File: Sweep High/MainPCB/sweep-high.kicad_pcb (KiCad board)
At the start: 2 copper layers, 229.5 x 95.2 mm, 64 parts, among them J1 AudioJack4dpb, J2 AudioJack4dpb, SW10 SW_Push, SW11 SW_Push, SW11_r1 SW_Push, SW12 SW_Push, SW12_r1 SW_Push, SW13_r1 SW_Push, SW14 SW_Push, SW15 SW_Push, SW15_r1 SW_Push, SW16 SW_Push, SW16_r1 SW_Push, SW17 SW_Push, SW17_r1 SW_Push, SW18 SW_Push, SW18_r1 SW_Push, SW2 SW_Push, SW2 SW_SPDT, SW20 SW_Push, SW20_r1 SW_Push, SW21 SW_Push, SW21_r1 SW_Push, SW2_r1 SW_Push, SW3 SW_Push, SW3_r1 SW_Push, SW4 SW_Push, SW4_r1 SW_Push, SW5 SW_Push, SW5_r1 SW_Push, SW6 SW_Push, SW6_r1 SW_Push, SW7_r1 SW_Push, SW8 SW_Push, SW8_r1 SW_Push, SW9 SW_Push, SW9_r1 SW_Push, U1 ProMicro-kbd, U2 ProMicro-kbd

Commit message: lots of worky
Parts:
- removed the H2 at (113.9, 55.8)
- removed H4: MountingHole, MountingHole:MountingHole_3.7mm
- removed the H5 at (54.2, 64.4)
- removed the H6 at (98.9, 119.8)
- removed the H8 at (62.1, 115.5)
- removed the SW2 at (140.6, 84.0)
- removed the SW2 at (160.9, 84.5)
- removed SW20_r1, SW21_r1: SW_Push, * duckyb-collection:keyswitch_cherrymx_alps_choc12_slots_1u
- added H0: MountingHole, MountingHole:MountingHole_3.2mm_M3, F.Cu at (99.4, 127.7)
- added H2: MountingHole, MountingHole:MountingHole_2.2mm_M2, F.Cu at (37.1, 242.3)
- added H2: MountingHole, MountingHole:MountingHole_3.2mm_M3, F.Cu at (112.1, 56.6)
- added H5: MountingHole, MountingHole:MountingHole_2.2mm_M2, F.Cu at (-21.6, 252.4)
- added H5: MountingHole, MountingHole:MountingHole_2.2mm_M2, B.Cu at (188.5, 56.6)
- added H6: MountingHole, MountingHole:MountingHole_2.2mm_M2, F.Cu at (24.4, 313.4)
- added H6: MountingHole, MountingHole:MountingHole_2.2mm_M2, B.Cu at (247.2, 66.7)
- added H8: MountingHole, MountingHole:MountingHole_2.2mm_M2, F.Cu at (-19.4, 307.3)
- added H8: MountingHole, MountingHole:MountingHole_2.2mm_M2, B.Cu at (245.0, 121.6)
- added SW10: SW_Push, Kailh:SW_PG1350_cut, F.Cu at (7.97, 263.6)
- added SW10_r1: SW_Push, kbd:CherryMX_Choc_1u, F.Cu at (169.3, 132.5)
- added SW11: SW_Push, Kailh:SW_PG1350_cut, F.Cu at (27.0, 268.2)
- added SW12: SW_Push, Kailh:SW_PG1350_cut, F.Cu at (45.9, 270.7)
- added SW14: SW_Push, Kailh:SW_PG1350_cut, F.Cu at (-30.0, 300.7)
- added SW14_r1: SW_Push, kbd:CherryMX_Choc_1u, F.Cu at (189.2, 124.4)
- added SW15: SW_Push, Kailh:SW_PG1350_cut, F.Cu at (-11.0, 288.9)
- added SW16: SW_Push, Kailh:SW_PG1350_cut, F.Cu at (7.97, 282.6)
- added SW17: SW_Push, Kailh:SW_PG1350_cut, F.Cu at (27.0, 287.2)
- added SW18: SW_Push, Kailh:SW_PG1350_cut, F.Cu at (45.9, 289.8)
- added SW2: SW_Push, Kailh:SW_PG1350_cut, F.Cu at (-30.0, 262.7)
- added SW2: SW_Push, Kailh:SW_PG1350_cut, F.Cu at (45.0, 77.0)
- added SW2: SW_Push, Kailh:SW_PG1350_cut, B.Cu at (255.6, 77.0)
- added SW20: SW_Push, Kailh:SW_PG1350_cut, F.Cu at (55.9, 318.2)
- added SW21: SW_Push, Kailh:SW_PG1350_cut, F.Cu at (36.2, 310.0)
- added SW3: SW_Push, Kailh:SW_PG1350_cut, F.Cu at (-11.0, 250.7)
- added SW4: SW_Push, Kailh:SW_PG1350_cut, F.Cu at (7.97, 244.6)
- added SW5: SW_Push, Kailh:SW_PG1350_cut, F.Cu at (27.0, 249.2)
- added SW6: SW_Push, Kailh:SW_PG1350_cut, F.Cu at (46.0, 251.7)
- added SW8: SW_Push, Kailh:SW_PG1350_cut, F.Cu at (-30.0, 281.7)
- added SW9: SW_Push, Kailh:SW_PG1350_cut, F.Cu at (-11.0, 269.8)
- ?: moved to B.Cu
- Bat+1, BatGND4: renamed from B-; footprint kbd:1pin_conn -> Connector_Pin:Pin_D1.4mm_L8.5mm_W2.8mm_FlatFork
- Bat+r1, BatGND1: renamed from B+; footprint kbd:1pin_conn -> Connector_Pin:Pin_D1.4mm_L8.5mm_W2.8mm_FlatFork
- H1, H3: footprint MountingHole:MountingHole_3.7mm -> MountingHole:MountingHole_3.2mm_M3
- H7: footprint MountingHole:MountingHole_3.7mm -> MountingHole:MountingHole_2.2mm_M2; moved to B.Cu
- J1, J2: footprint Kailh:TRRS-PJ-DPB2 -> Connector_Audio:Jack_3.5mm_PJ320D_Horizontal
- RSW1 (x2), RSW2 (x2): footprint kbd:SW_SPST_B3U-1000P -> Button_Switch_SMD:SW_SPST_B3U-1000P
- SW10, SW11, SW11_r1, SW12, SW12_r1, SW13_r1, SW14, SW15, SW15_r1, SW16, SW16_r1, SW17, SW17_r1, SW18, SW18_r1, SW2, SW20, SW21, SW2_r1, SW3, SW3_r1, SW4, SW4_r1, SW5, SW5_r1, SW6, SW6_r1, SW7_r1, SW8, SW8_r1, SW9, SW9_r1: footprint * duckyb-collection:keyswitch_cherrymx_alps_choc12_slots_1u -> kbd:CherryMX_Choc_1u
- SW_POWER1, SW_POWERR1: footprint Kailh:SPDT_C128955 -> Button_Switch_SMD:SW_SPDT_PCM12
- moved ? 183.1 mm to (245.0, 121.6), turned to 180 degrees
- moved H3 157.6 mm to (53.4, 66.7)
- moved H1 147.0 mm to (55.6, 121.6)
- moved G*** 133.8 mm to (82.0, 118.1)
- moved H7 39.3 mm to (201.2, 127.7), turned to 180 degrees
- moved SW_POWER1 20.4 mm to (140.4, 84.1), turned to 0 degrees
- moved SW_POWERR1 20.1 mm to (160.8, 84.1), turned to 0 degrees
- moved J2 13.3 mm to (159.4, 119.7), turned to 0 degrees
- moved J1 13.3 mm to (141.1, 119.7), turned to 180 degrees
- moved Bat+1 0.29 mm to (134.7, 83.5)
- moved BatGND1 0.29 mm to (146.2, 83.5)
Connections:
- Bat+1 pad 1: gnd -> BT+
- Bat+r1 pad 1: BT+ -> BT+_r
- BatGND1 pad 1: BT+_r -> gnd
- J1 pad R1: Switch18_r -> vcc
- J1 pad R2: vcc -> gnd
- J1 pad S: gnd -> Switch18
- J1 pad T: gnd -> unconnected-(J1-PadT)
- J2 pad R1: Switch18 -> vcc
- J2 pad R2: vcc -> gnd
- J2 pad S: gnd -> Switch18_r
- J2 pad T: gnd -> unconnected-(J2-PadT)
- SW11_r1 pad 1: Switch9_r -> Switch10_r
- SW12_r1 pad 1: Switch10_r -> Switch11_r
- SW13_r1 pad 1: Switch11_r -> Switch12_r
- SW15_r1 pad 1: Switch13_r -> Switch14_r
- SW16_r1 pad 1: Switch14_r -> Switch15_r
- SW17_r1 pad 1: Switch15_r -> Switch16_r
- SW18_r1 pad 1: Switch12_r -> Switch17_r
- SW20 pad 1: Switch17 -> Switch16
- SW21 pad 1: Switch16 -> Switch17
- SW_POWER1 pad 1: Net-(SW_POWER1-Pad1) -> unconnected-(SW_POWER1-Pad1)
- SW_POWERR1 pad 1: Net-(SW_POWERR1-Pad1) -> unconnected-(SW_POWERR1-Pad1)
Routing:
- net Switch11_r: track 108.0 -> 17.6 mm
- net Switch3_r: track 89.5 -> 148.6 mm
- net Switch9_r: track 83.3 -> 30.6 mm
- net Switch12_r: track 80.5 -> 132.0 mm
- net Switch17_r: track 27.1 -> 73.9 mm
- net gnd: track 5.95 -> 47.3 mm, vias 0 -> 2
- net Switch17: track 33.7 -> 63.9 mm
- net Switch14_r: track 38.0 -> 64.0 mm
- net Switch6_r: track 154.4 -> 128.7 mm, vias 0 -> 1
- net Switch6: track 124.0 -> 148.0 mm
- net Switch2_r: track 108.7 -> 131.9 mm, vias 0 -> 1
- net Switch10_r: track 15.6 -> 38.2 mm
- net Switch7_r: track 131.7 -> 110.2 mm, vias 0 -> 1
- net Switch16_r: track 36.6 -> 15.3 mm
- net Switch7: track 103.1 -> 122.0 mm
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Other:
- board size 229.5 x 95.2 mm -> 304.6 x 280.9 mm
- rule pad_to_mask_clearance: 0 -> 0.051

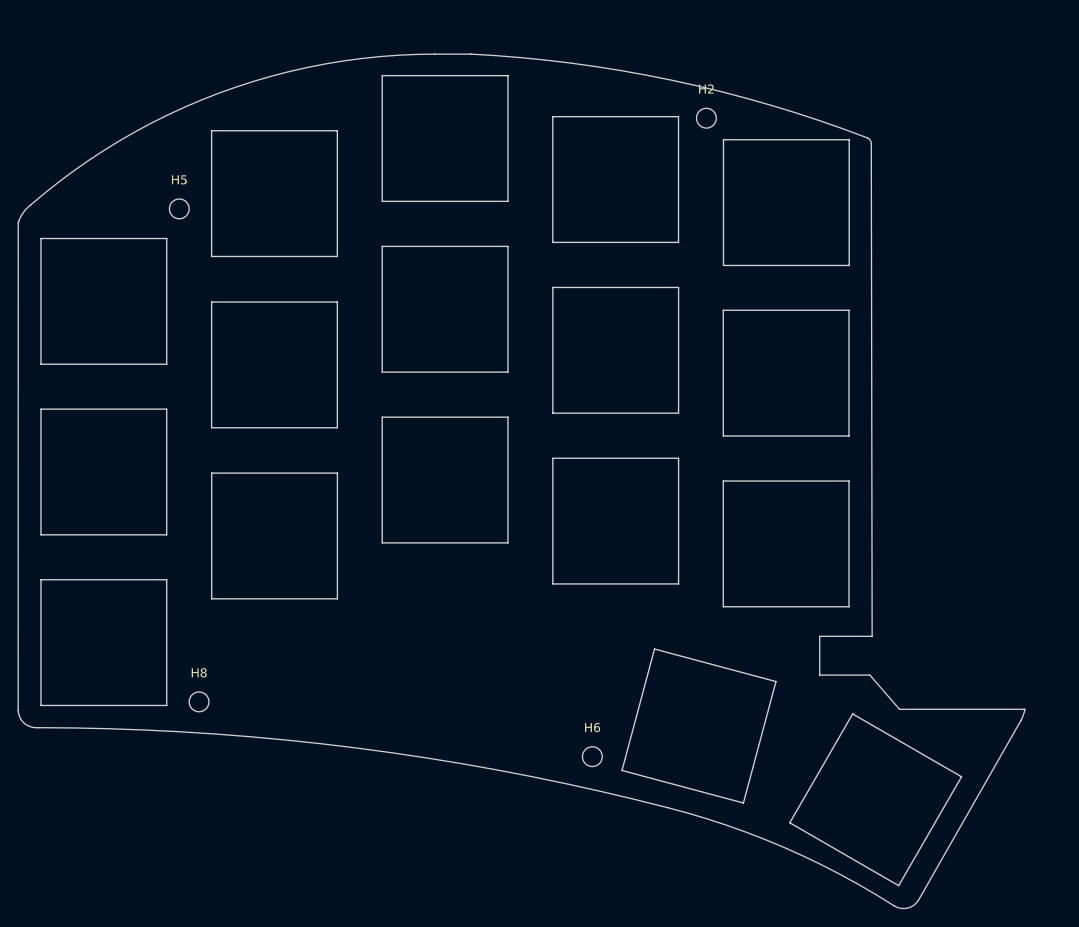
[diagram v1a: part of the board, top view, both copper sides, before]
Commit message: forgot to delete switgch plate form main PCB
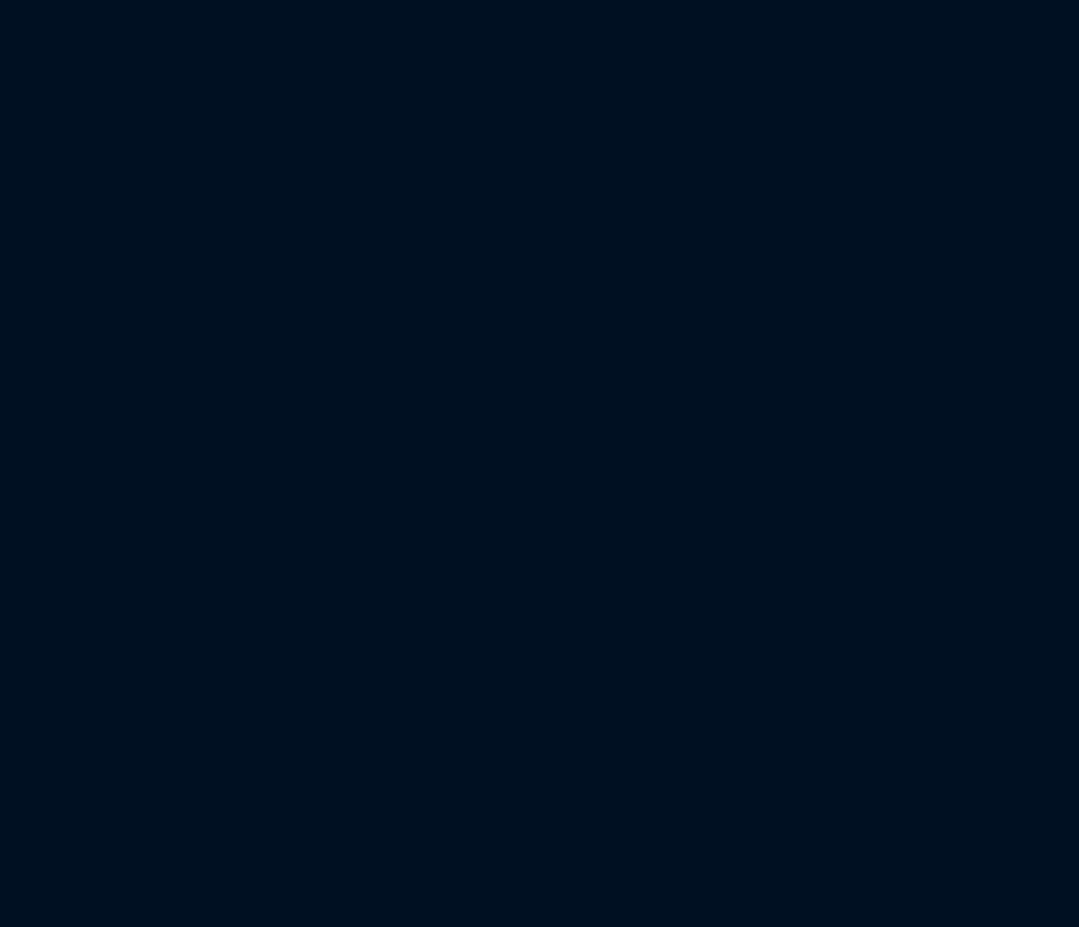
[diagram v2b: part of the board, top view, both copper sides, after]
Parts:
- removed the H2 at (37.1, 242.3)
- removed the H5 at (-21.6, 252.4)
- removed the H6 at (24.4, 313.4)
- removed the H8 at (-19.4, 307.3)
- removed the SW10 at (7.97, 263.6)
- removed the SW11 at (27.0, 268.2)
- removed the SW12 at (45.9, 270.7)
- removed the SW14 at (-30.0, 300.7)
- removed the SW15 at (-11.0, 288.9)
- removed the SW16 at (7.97, 282.6)
- removed the SW17 at (27.0, 287.2)
- removed the SW18 at (45.9, 289.8)
- removed the SW2 at (-30.0, 262.7)
- removed the SW20 at (55.9, 318.2)
- removed the SW21 at (36.2, 310.0)
- removed the SW3 at (-11.0, 250.7)
- removed the SW4 at (7.97, 244.6)
- removed the SW5 at (27.0, 249.2)
- removed the SW6 at (46.0, 251.7)
- removed the SW8 at (-30.0, 281.7)
- removed the SW9 at (-11.0, 269.8)
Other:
- board size 304.6 x 280.9 mm -> 229.5 x 95.2 mm

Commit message: more missed corrections
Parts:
- removed ?: , 
- removed the SW2 at (45.0, 77.0)
- removed the SW2 at (255.6, 77.0)
- H5, H6, H7, H8: footprint MountingHole:MountingHole_2.2mm_M2 -> MountingHole:MountingHole_3.2mm_M3
- renumbered H0 to H4
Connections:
- U1 pad 10: Switch1 -> Switch15
- U1 pad 9: Switch15 -> Switch1
- U2 pad 10: Switch1_r -> Switch15_r
- U2 pad 9: Switch15_r -> Switch1_r
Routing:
- net Switch12_r: track 132.0 -> 130.4 mm
